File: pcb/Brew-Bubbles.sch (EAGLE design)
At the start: 9 parts, among them U1 GP1A57HR, U2 WEMOS-D1-MINI

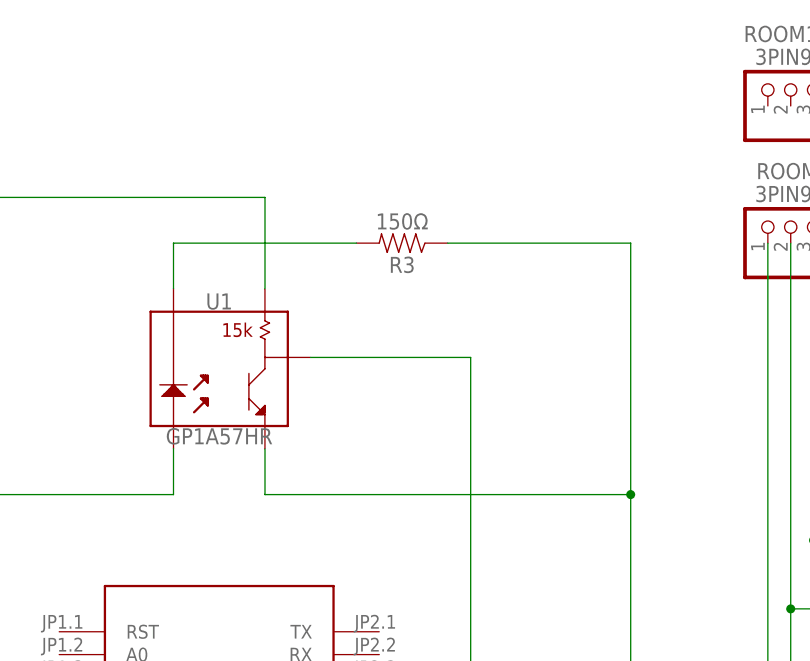
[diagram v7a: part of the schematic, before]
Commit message: Add in decoupling cap for sensor
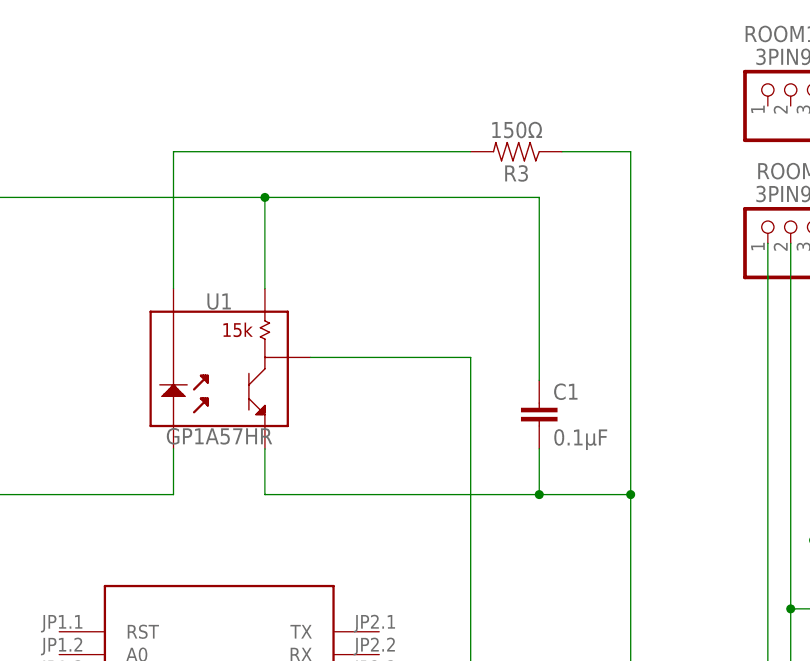
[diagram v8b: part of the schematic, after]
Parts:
- added C1: 0.1μF, rcl:C-EU025-024X044
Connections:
- net 3V3: now also C1.1
- net GND: now also C1.2
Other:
- moved on the sheet: R3
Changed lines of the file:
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@@
 <part name="ROOM1" library="pinhead" library_urn="urn:adsk.eagle:library:325" deviceset="PINHD-1X3" device="/90" package3d_urn="urn:adsk.eagle:package:22459/2" value="3PIN90"/>
 <part name="VESSEL1" library="pinhead" library_urn="urn:adsk.eagle:library:325" deviceset="PINHD-1X3" device="/90" package3d_urn="urn:adsk.eagle:package:22459/2" value="3PIN90"/>
+<part name="C1" library="rcl" library_urn="urn:adsk.eagle:library:334" deviceset="C-EU" device="025-024X044" package3d_urn="urn:adsk.eagle:package:23630/1" value="0.1μF"/>
 </parts>
 <sheets>
@@
 <attribute name="VALUE" x="17.78" y="86.106" size="1.778" layer="96" font="vector" align="top-center"/>
 </instance>
-<instance part="R3" gate="G$1" x="38.1" y="106.68" smashed="yes" rot="R180">
-<attribute name="NAME" x="38.1" y="105.156" size="1.778" layer="95" font="vector" rot="R180" align="bottom-center"/>
-<attribute name="VALUE" x="38.1" y="108.204" size="1.778" layer="96" font="vector" rot="R180" align="top-center"/>
+<instance part="R3" gate="G$1" x="50.8" y="116.84" smashed="yes" rot="R180">
+<attribute name="NAME" x="50.8" y="115.316" size="1.778" layer="95" font="vector" rot="R180" align="bottom-center"/>
+<attribute name="VALUE" x="50.8" y="118.364" size="1.778" layer="96" font="vector" rot="R180" align="top-center"/>
 </instance>
 <instance part="ROOM" gate="A" x="81.28" y="109.22" smashed="yes" rot="R90">
@@
 <attribute name="VALUE" x="123.19" y="128.27" size="1.778" layer="96" rot="R180"/>
 <attribute name="NAME" x="122.428" y="130.81" size="1.778" layer="95" rot="R180"/>
+</instance>
+<instance part="C1" gate="G$1" x="53.34" y="88.9" smashed="yes">
+<attribute name="NAME" x="54.864" y="89.281" size="1.778" layer="95"/>
+<attribute name="VALUE" x="54.864" y="84.201" size="1.778" layer="96"/>
 </instance>
 </instances>
@@
 <wire x1="-12.7" y1="45.72" x2="-12.7" y2="27.94" width="0.1524" layer="91"/>
 <junction x="-12.7" y="45.72"/>
+<junction x="22.86" y="111.76"/>
+<wire x1="22.86" y1="111.76" x2="53.34" y2="111.76" width="0.1524" layer="91"/>
+<pinref part="C1" gate="G$1" pin="1"/>
+<wire x1="53.34" y1="111.76" x2="53.34" y2="91.44" width="0.1524" layer="91"/>
 </segment>
 </net>
@@
 <wire x1="22.86" y1="83.82" x2="22.86" y2="78.74" width="0.1524" layer="91"/>
 <wire x1="63.5" y1="48.26" x2="63.5" y2="78.74" width="0.1524" layer="91"/>
-<wire x1="63.5" y1="78.74" x2="63.5" y2="106.68" width="0.1524" layer="91"/>
+<wire x1="63.5" y1="78.74" x2="63.5" y2="116.84" width="0.1524" layer="91"/>
 <junction x="63.5" y="78.74"/>
-<wire x1="22.86" y1="78.74" x2="63.5" y2="78.74" width="0.1524" layer="91"/>
-<wire x1="43.18" y1="106.68" x2="63.5" y2="106.68" width="0.1524" layer="91"/>
+<wire x1="22.86" y1="78.74" x2="53.34" y2="78.74" width="0.1524" layer="91"/>
+<wire x1="53.34" y1="78.74" x2="63.5" y2="78.74" width="0.1524" layer="91"/>
+<wire x1="55.88" y1="116.84" x2="63.5" y2="116.84" width="0.1524" layer="91"/>
 <wire x1="116.84" y1="48.26" x2="116.84" y2="106.68" width="0.1524" layer="91"/>
 <wire x1="63.5" y1="48.26" x2="78.74" y2="48.26" width="0.1524" layer="91"/>
@@
 <wire x1="78.74" y1="48.26" x2="78.74" y2="106.68" width="0.1524" layer="91"/>
 <junction x="78.74" y="48.26"/>
+<pinref part="C1" gate="G$1" pin="2"/>
+<wire x1="53.34" y1="83.82" x2="53.34" y2="78.74" width="0.1524" layer="91"/>
+<junction x="53.34" y="78.74"/>
 </segment>
 </net>
@@
 <pinref part="U1" gate="G$1" pin="2"/>
 <pinref part="R3" gate="G$1" pin="2"/>
-<wire x1="33.02" y1="106.68" x2="12.7" y2="106.68" width="0.1524" layer="91"/>
-<wire x1="12.7" y1="106.68" x2="12.7" y2="101.6" width="0.1524" layer="91"/>
+<wire x1="45.72" y1="116.84" x2="12.7" y2="116.84" width="0.1524" layer="91"/>
+<wire x1="12.7" y1="116.84" x2="12.7" y2="101.6" width="0.1524" layer="91"/>
 </segment>
 </net>
@@
 packages will not be understood (or retained) with this version.
 </note>
+<note version="8.4" severity="warning">
+Since Version 8.4, EAGLE supports properties for SPICE simulation.
+Probes in schematics and SPICE mapping objects found in parts and library devices
+will not be understood with this version. Update EAGLE to the latest version
+for full support of SPICE simulation.
+</note>
 </compatibility>
